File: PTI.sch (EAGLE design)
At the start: 48 parts, among them J1 GPIO, J2 Micro USB, J3 Micro USB, T1 MMUN2133LT1G, U1 MCP73871, U2 TPS61090RSAR, U3 MAX1704X

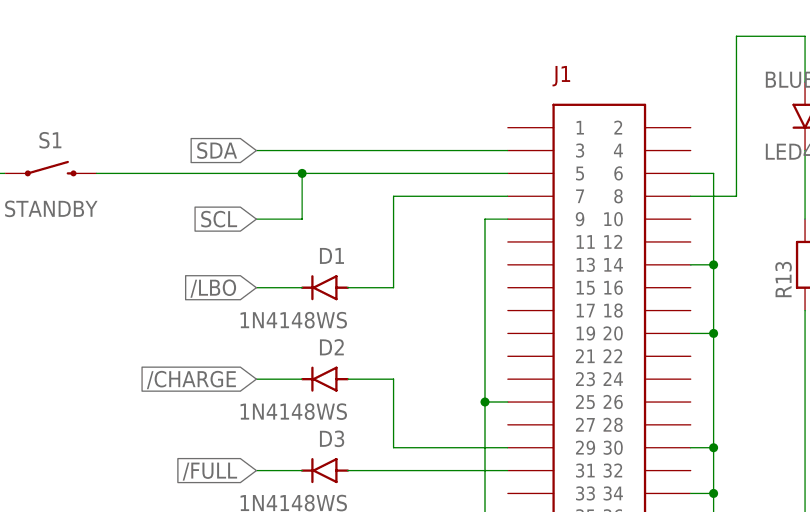
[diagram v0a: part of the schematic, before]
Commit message: Rev B adds 2mm to the left side of the board to facilitate USB connections.
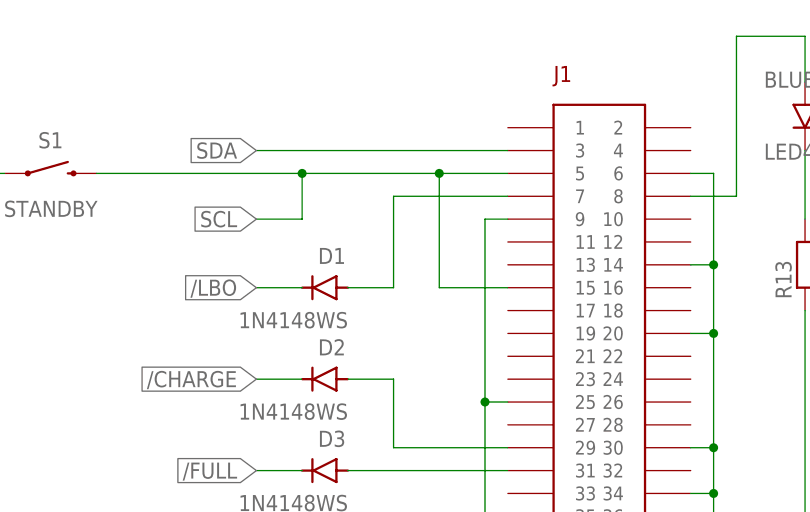
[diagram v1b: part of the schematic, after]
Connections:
- net SCL: now also J1.15
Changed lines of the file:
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@@
 <pinref part="S1" gate="G$1" pin="2"/>
 <label x="190.5" y="185.42" size="1.778" layer="95" rot="MR0" xref="yes"/>
-<wire x1="218.44" y1="190.5" x2="195.58" y2="190.5" width="0.1524" layer="91"/>
+<wire x1="218.44" y1="190.5" x2="210.82" y2="190.5" width="0.1524" layer="91"/>
+<wire x1="210.82" y1="190.5" x2="195.58" y2="190.5" width="0.1524" layer="91"/>
 <wire x1="195.58" y1="190.5" x2="172.72" y2="190.5" width="0.1524" layer="91"/>
 <wire x1="190.5" y1="185.42" x2="195.58" y2="185.42" width="0.1524" layer="91"/>
 <wire x1="195.58" y1="185.42" x2="195.58" y2="190.5" width="0.1524" layer="91"/>
 <junction x="195.58" y="190.5"/>
+<pinref part="J1" gate="G$1" pin="15"/>
+<wire x1="218.44" y1="177.8" x2="210.82" y2="177.8" width="0.1524" layer="91"/>
+<wire x1="210.82" y1="177.8" x2="210.82" y2="190.5" width="0.1524" layer="91"/>
+<junction x="210.82" y="190.5"/>
 </segment>
 </net>

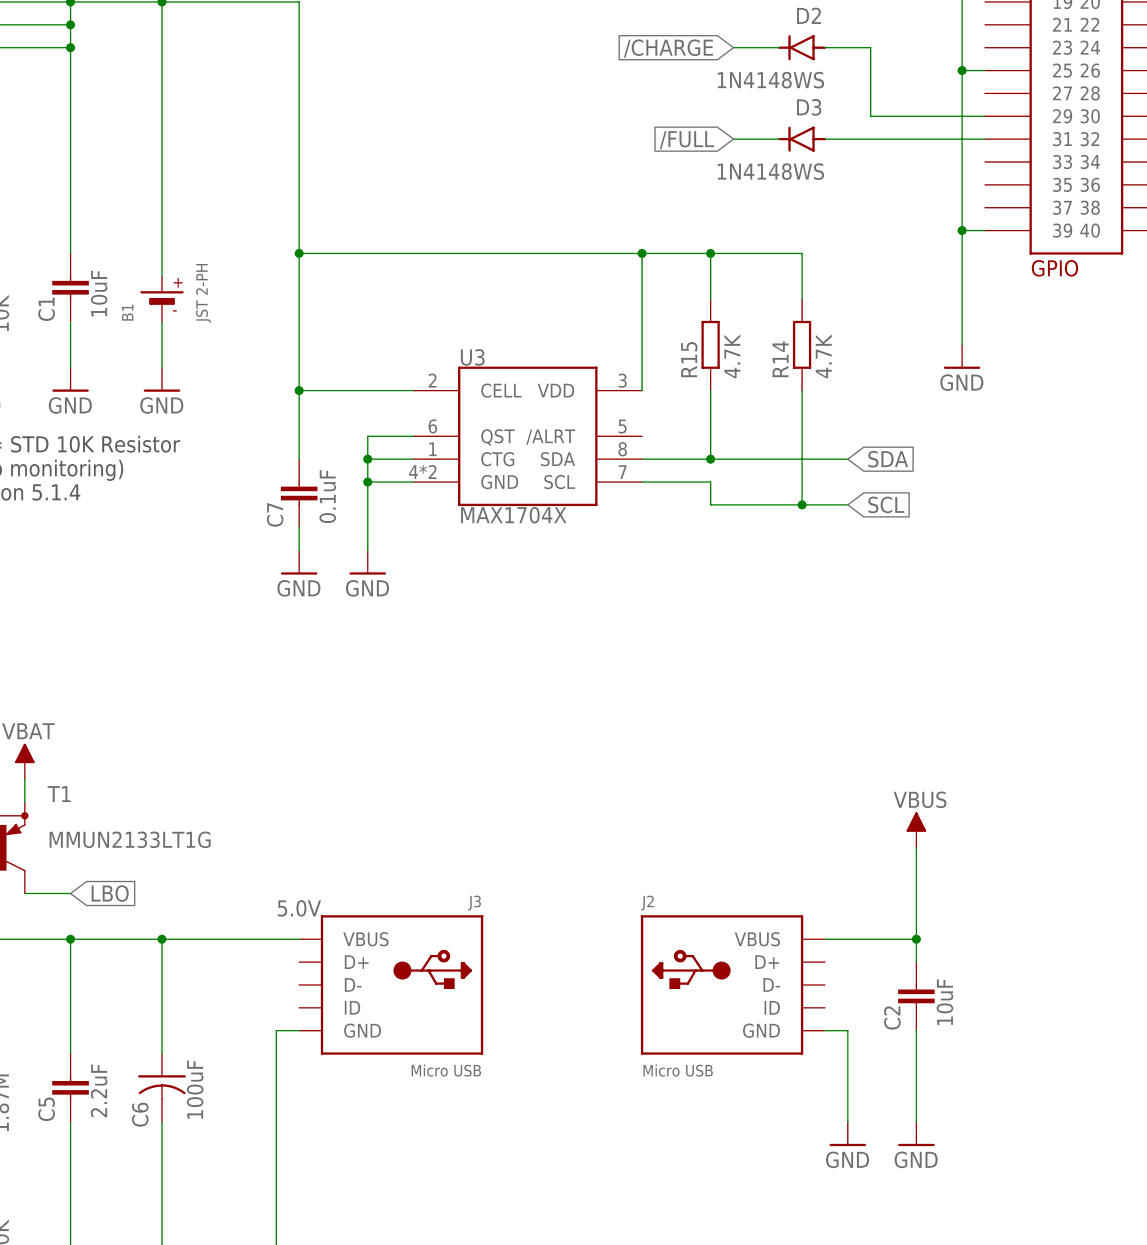
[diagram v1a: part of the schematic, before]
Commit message: Routes GPIO13 (pin 33 on J1) to the ID pin on J3 (power out to USB manifold).  This GPIO can be used to toggle on/off a MOSFET on the USB manifold used to enable or disable receiver 5V power bus.
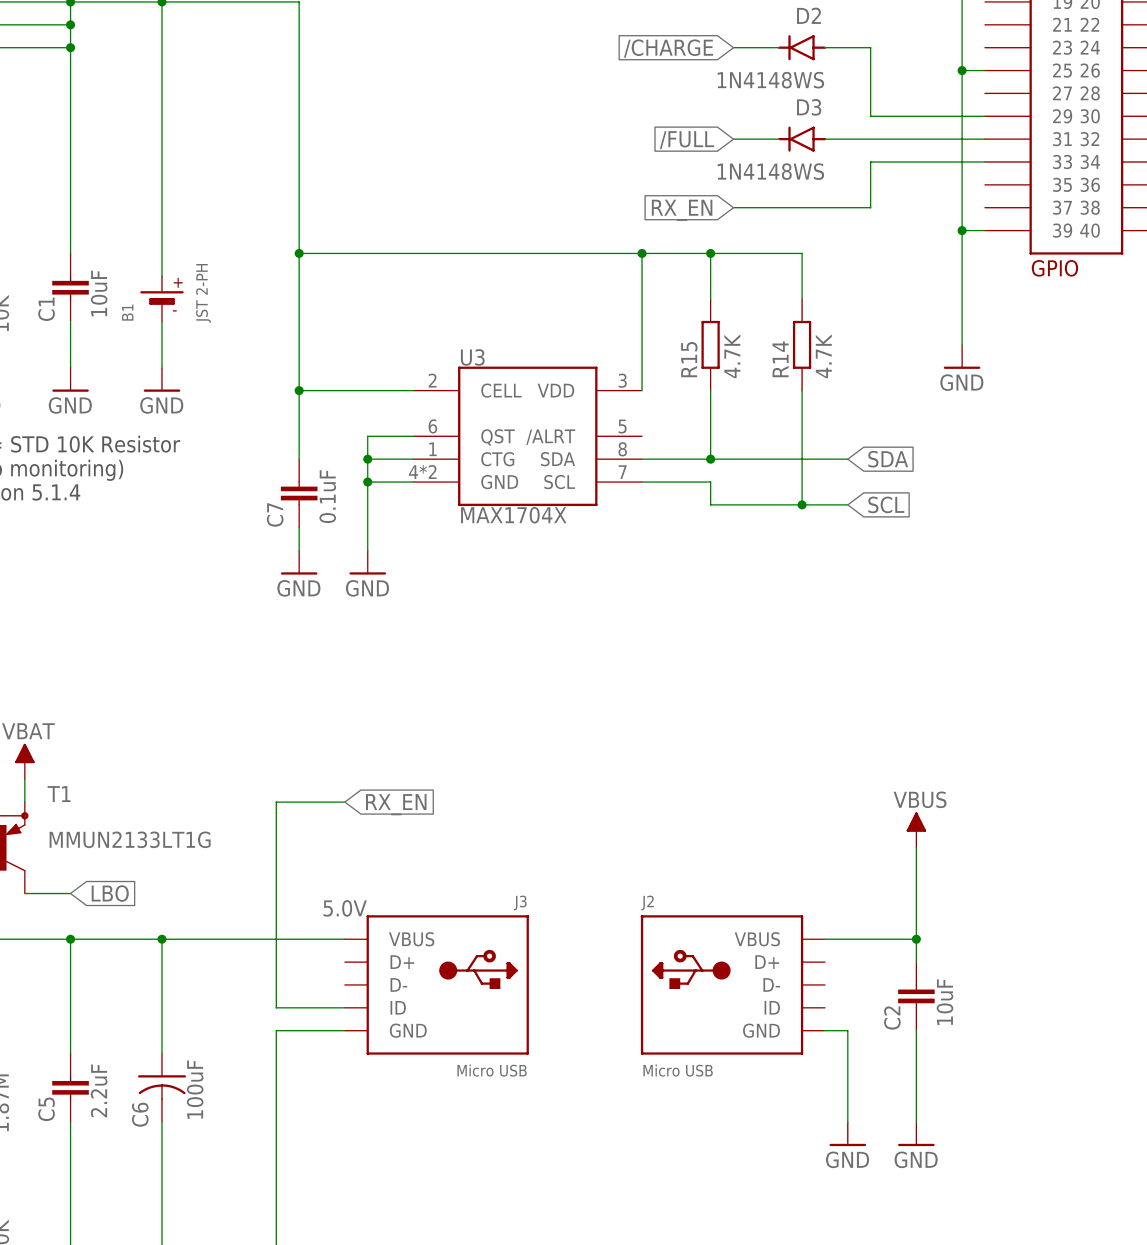
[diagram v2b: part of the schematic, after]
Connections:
- new net RX_EN: J1.33, J3.ID
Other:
- moved on the sheet: J3
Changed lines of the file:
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@@
 <?xml version="1.0" encoding="utf-8"?>
 <!DOCTYPE eagle SYSTEM "eagle.dtd">
-<eagle version="9.4.2">
+<eagle version="9.5.1">
 <drawing>
 <settings>
@@
 <attributes>
 <attribute name="DWG_NUMBER" value="CKT-1000"/>
-<attribute name="REV" value="-"/>
+<attribute name="REV" value="C"/>
 <attribute name="TITLE" value="PIMTECTOR INTERFACE BOARD"/>
 </attributes>
@@
 <instance part="MH3" gate="G$1" x="243.84" y="48.26" smashed="yes"/>
 <instance part="MH4" gate="G$1" x="248.92" y="48.26" smashed="yes"/>
-<instance part="J3" gate="G$1" x="152.4" y="63.5" smashed="yes" rot="MR0">
-<attribute name="NAME" x="162.56" y="72.136" size="1.27" layer="95" rot="MR0"/>
-<attribute name="VALUE" x="162.56" y="53.34" size="1.27" layer="96" rot="MR0"/>
+<instance part="J3" gate="G$1" x="157.48" y="63.5" smashed="yes" rot="MR0">
+<attribute name="NAME" x="167.64" y="72.136" size="1.27" layer="95" rot="MR0"/>
+<attribute name="VALUE" x="167.64" y="53.34" size="1.27" layer="96" rot="MR0"/>
 </instance>
 <instance part="GND24" gate="1" x="149.86" y="109.22" smashed="yes">
@@
 <segment>
 <pinref part="J3" gate="G$1" pin="GND"/>
-<wire x1="142.24" y1="58.42" x2="139.7" y2="58.42" width="0.1524" layer="91"/>
+<wire x1="147.32" y1="58.42" x2="139.7" y2="58.42" width="0.1524" layer="91"/>
 <pinref part="GND23" gate="1" pin="GND"/>
 <wire x1="139.7" y1="58.42" x2="139.7" y2="25.4" width="0.1524" layer="91"/>
@@
 <wire x1="91.44" y1="68.58" x2="106.68" y2="68.58" width="0.1524" layer="91"/>
 <junction x="106.68" y="68.58"/>
-<wire x1="142.24" y1="68.58" x2="127" y2="68.58" width="0.1524" layer="91"/>
+<wire x1="147.32" y1="68.58" x2="127" y2="68.58" width="0.1524" layer="91"/>
 <junction x="127" y="68.58"/>
-<label x="139.7" y="71.12" size="1.778" layer="95"/>
+<label x="144.78" y="71.12" size="1.778" layer="95"/>
 <pinref part="J3" gate="G$1" pin="VBUS"/>
 </segment>
@@
 </segment>
 </net>
+<net name="RX_EN" class="0">
+<segment>
+<pinref part="J3" gate="G$1" pin="ID"/>
+<wire x1="147.32" y1="60.96" x2="139.7" y2="60.96" width="0.1524" layer="91"/>
+<wire x1="139.7" y1="60.96" x2="139.7" y2="83.82" width="0.1524" layer="91"/>
+<wire x1="139.7" y1="83.82" x2="147.32" y2="83.82" width="0.1524" layer="91"/>
+<label x="147.32" y="83.82" size="1.778" layer="95" xref="yes"/>
+</segment>
+<segment>
+<pinref part="J1" gate="G$1" pin="33"/>
+<wire x1="218.44" y1="154.94" x2="205.74" y2="154.94" width="0.1524" layer="91"/>
+<wire x1="205.74" y1="154.94" x2="205.74" y2="149.86" width="0.1524" layer="91"/>
+<wire x1="205.74" y1="149.86" x2="190.5" y2="149.86" width="0.1524" layer="91"/>
+<label x="190.5" y="149.86" size="1.778" layer="95" rot="R180" xref="yes"/>
+</segment>
+</net>
